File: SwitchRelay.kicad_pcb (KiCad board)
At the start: 2 copper layers, 50 x 33 mm, 13 parts, among them J1 Decoder, J2 Switch, J3 Point, J4 AUX, K1 HFD2_xxx-x-L2

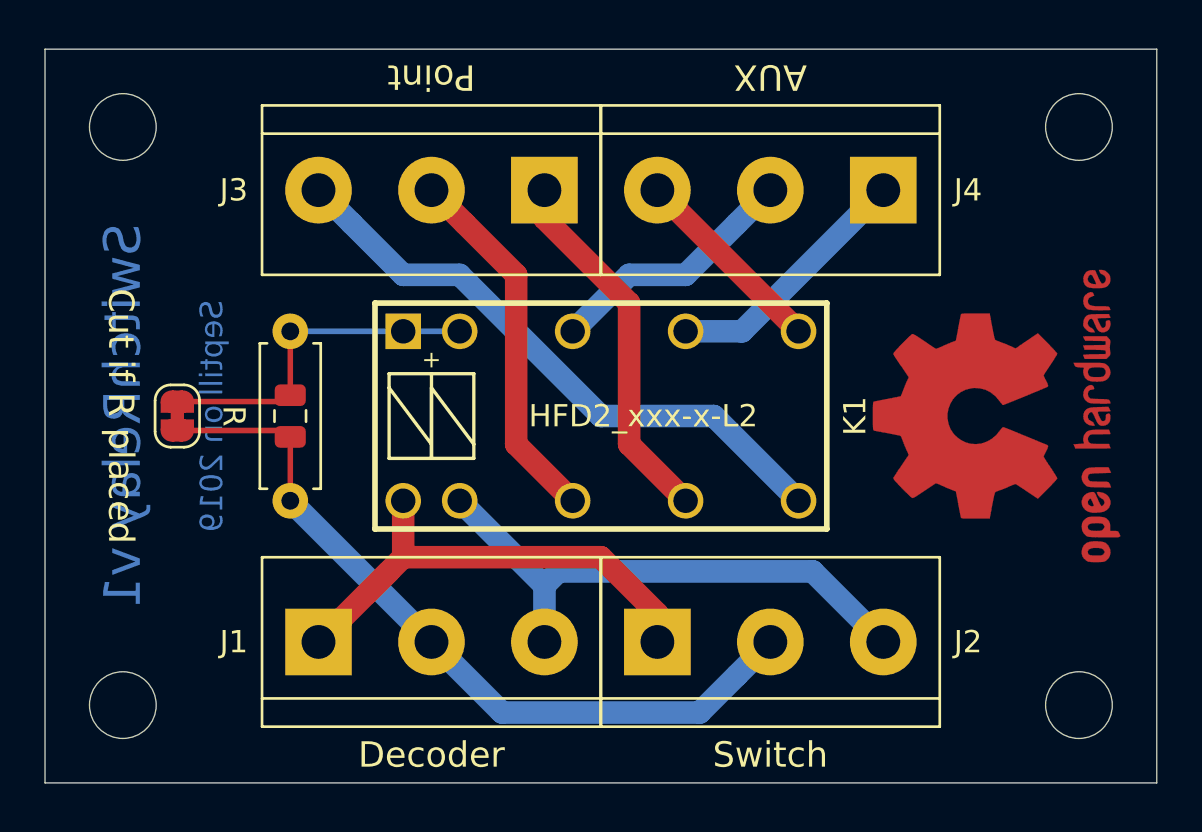
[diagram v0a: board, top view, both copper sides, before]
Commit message: Made version 2 with RT314F24
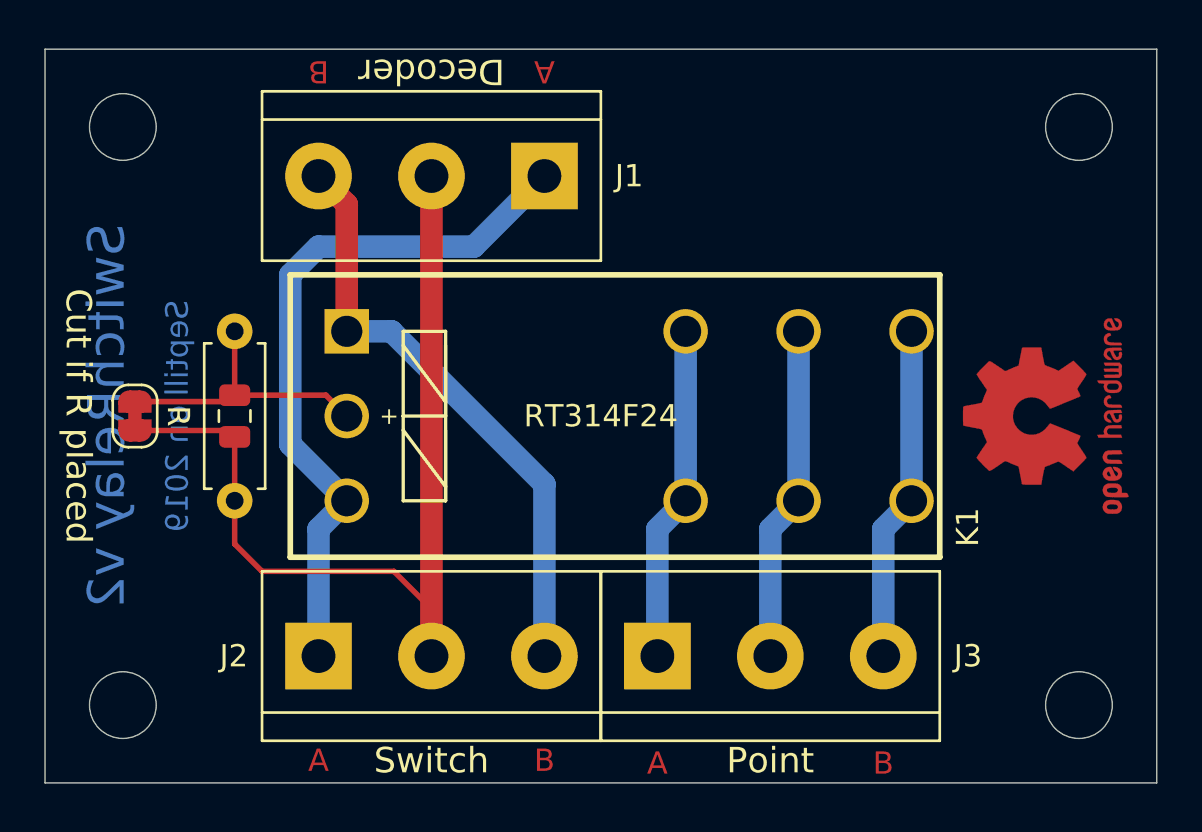
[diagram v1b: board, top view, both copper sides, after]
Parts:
- removed J4: AUX, TerminalBlock:TerminalBlock_bornier-3_P5.08mm
- K1: value HFD2_xxx-x-L2 -> RT314F24; footprint septillion_relay:HFD2_xxx-x-L2 -> septillion_relay:RTxxxFxx
- REF**: value OSHW-Logo2_14.6x12mm_Copper -> OSHW-Logo2_9.8x8mm_Copper; footprint Symbol:OSHW-Logo2_14.6x12mm_Copper -> Symbol:OSHW-Logo2_9.8x8mm_Copper
- moved J1 23.3 mm to (139.1, 105.4), turned to 180 degrees
- moved J3 21.6 mm to (144.1, 127.0), turned to 0 degrees
- moved J2 15.3 mm to (128.9, 127.0)
- moved R1 2.50 mm to (125.1, 112.4)
- moved R2 2.50 mm to (125.1, 116.2)
- moved REF** 2.22 mm to (161.6, 116.2)
- moved JP1 1.91 mm to (120.7, 116.2)
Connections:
- K1 pad 11: Net-(J3-Pad1) -> Net-(J3-Pad2)
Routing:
- net Net-(J3-Pad3): track 27.4 -> 15.1 mm
- net /AUX-R: track 11.5 -> 0.00 mm
- net /AUX-C: track 11.5 -> 0.00 mm
- net /AUX-S: track 8.98 -> 0.00 mm
- net Net-(J1-Pad1): track 23.0 -> 32.0 mm
- net Net-(J1-Pad2): track 34.9 -> 43.2 mm
- net Net-(JP1-Pad2): track 15.7 -> 12.9 mm
- net Net-(J1-Pad3): track 24.7 -> 27.0 mm
- net Net-(J3-Pad1): track 16.6 -> 15.1 mm
- net Net-(J3-Pad2): track 16.6 -> 15.1 mm
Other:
- board text added: "Max. 16A"
- board text added: "SwitchRelay v2"
- board text removed: "Max. 30V 3A"
- board text removed: "SwitchRelay v1"

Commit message: Small changes
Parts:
- K1: value RT314F24 -> RT314Fxx
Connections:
- K1 pad A1: Net-(J1-Pad3) -> Net-(J1-Pad1)
- K1 pad A2: Net-(J1-Pad1) -> Net-(J1-Pad3)
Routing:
- net Net-(J1-Pad1): track 32.0 -> 29.5 mm
- net Net-(J1-Pad3): track 27.0 -> 29.0 mm
